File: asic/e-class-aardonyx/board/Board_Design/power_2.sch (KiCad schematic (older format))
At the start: 36 parts, among them Q1 FDN339AN, SW2 FSM2JSMAATR, U10 TPS7A7002DDAR, U11 ADM1085, U12 ADM1085, U13 TPS7A7002DDAR, U14 74AUP1G09GW

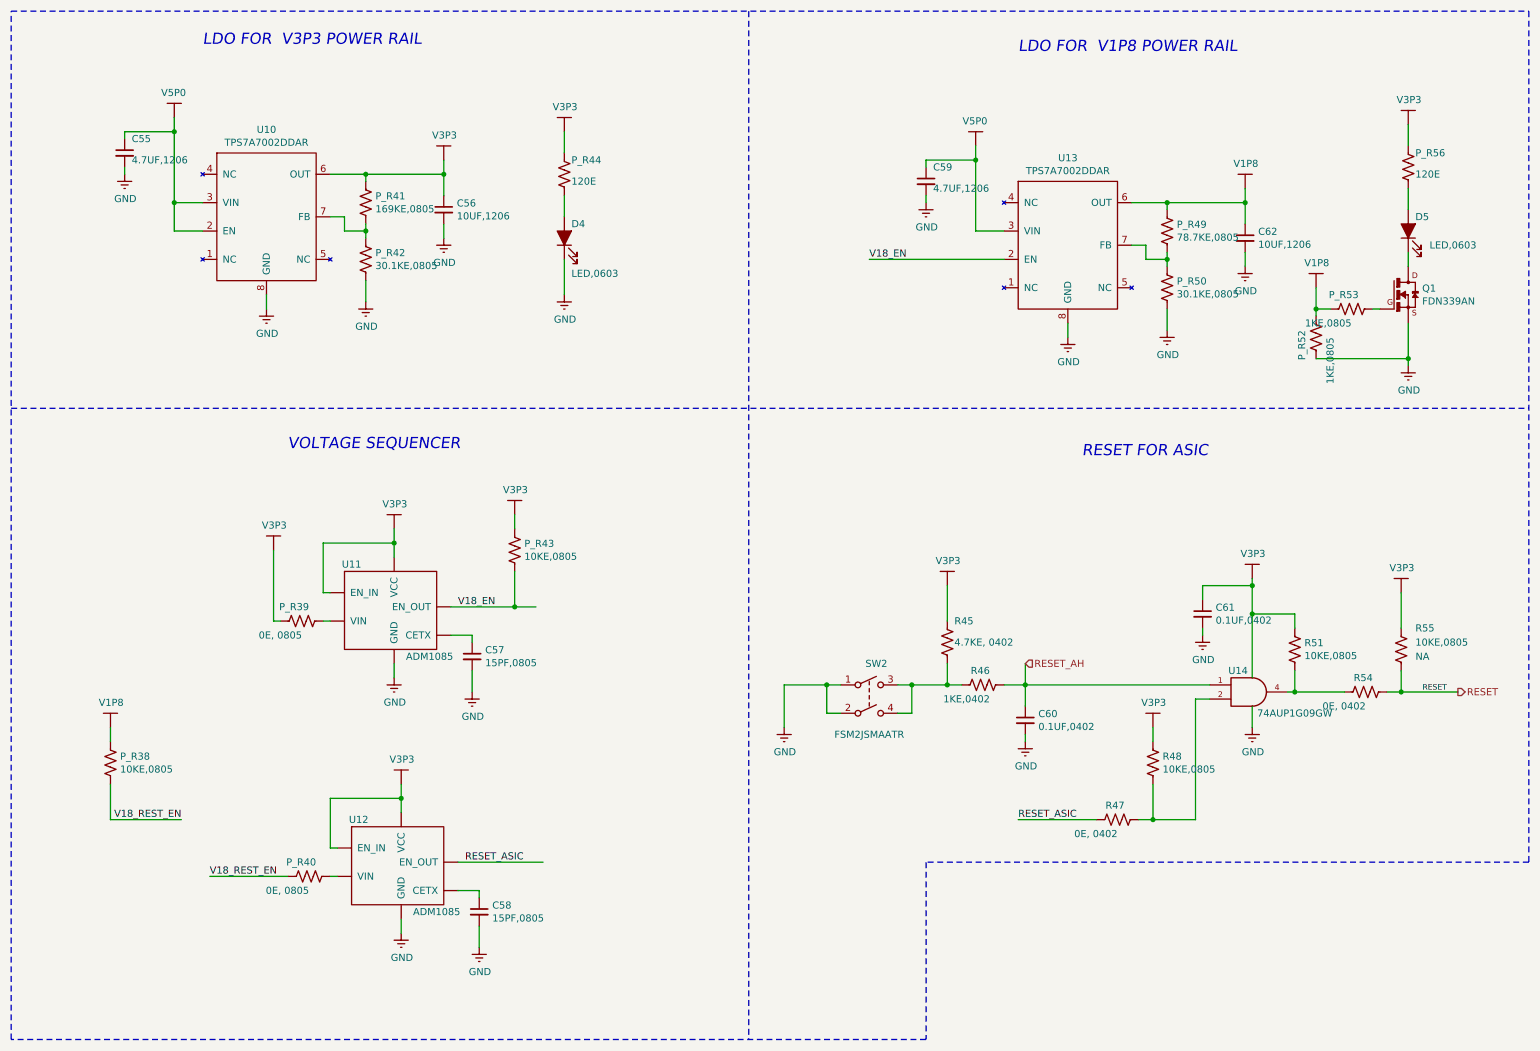
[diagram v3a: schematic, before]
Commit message: updated commented pending schematic
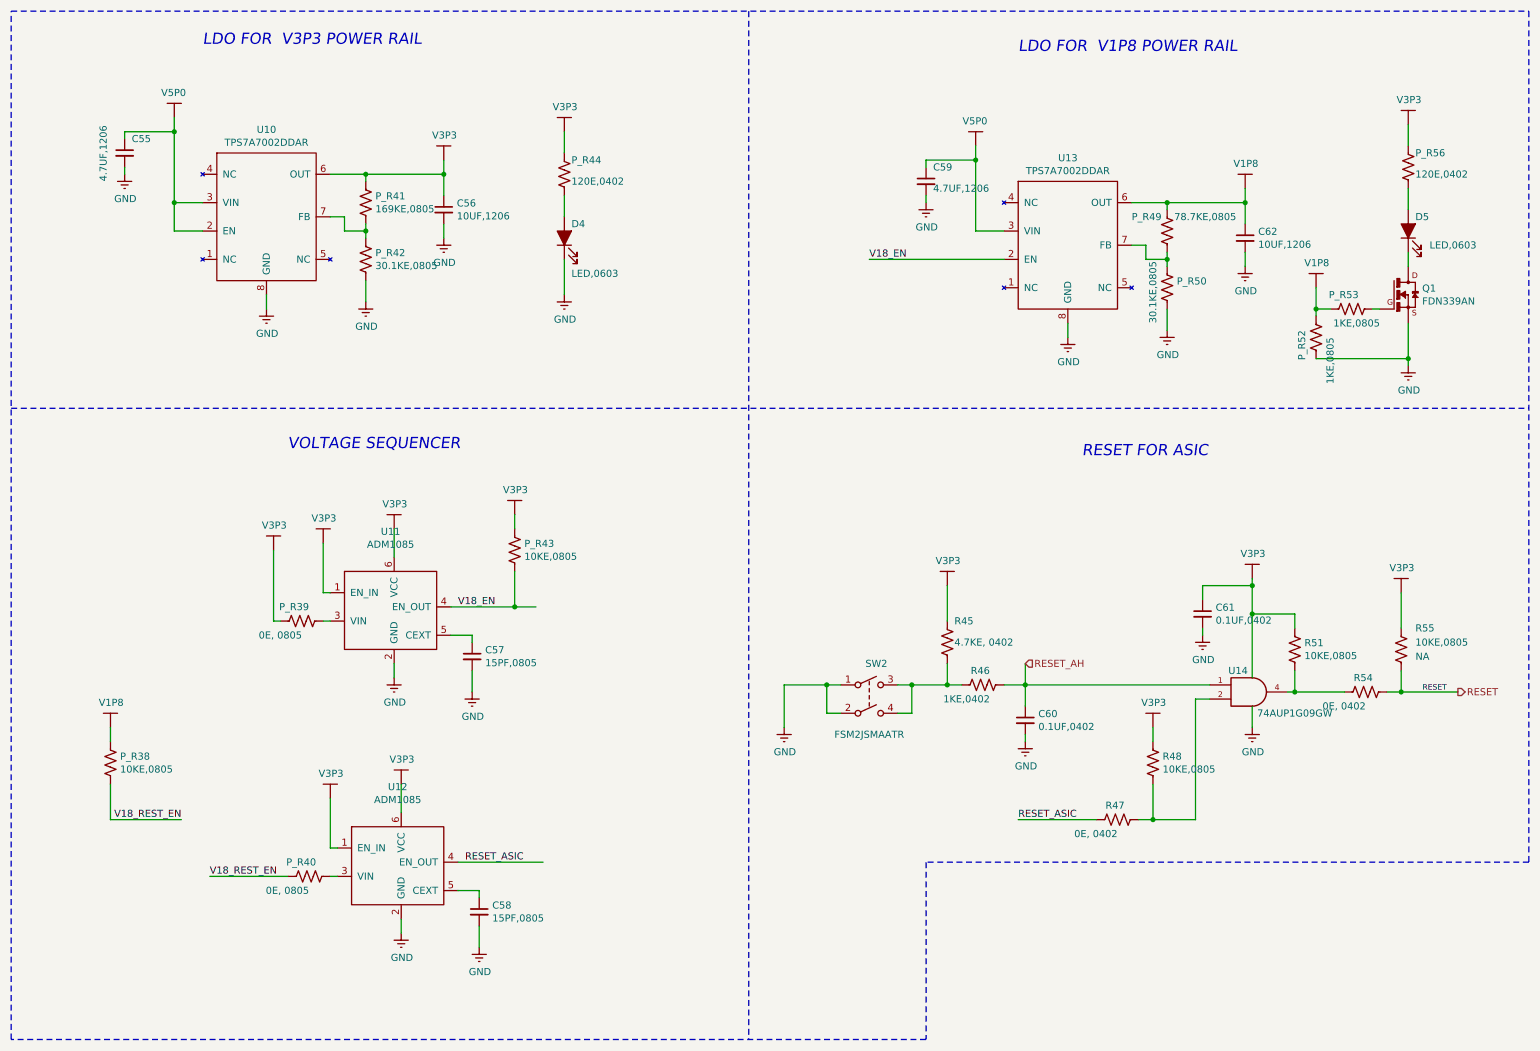
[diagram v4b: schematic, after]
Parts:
- removed U11, U12: ADM1085, symbol Aardonyx-rescue:ADM1085-aardonyx
- added U11, U12: ADM1085, symbol Aardonyx-rescue:ADM1085-skt32e_asic
- P_R44, P_R56: value 120E -> 120E,0402; Description RES SMD 120 OHM 5% 1/4W 1206 -> RES SMD 120 OHM 1% 1/16W 0402; Digikey PartNumber 311-120ERCT-ND -> 311-120LRCT-ND; Manufactured Part Number RC1206JR-07120RL -> RC0402FR-07120RL
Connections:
- net GND: now also U11.2 (GND), U12.2 (GND)
- net RESET_ASIC: now also U12.4 (EN_OUT)
- net V18_EN: now also U11.4 (EN_OUT)
- net at C57.1: now also U11.5 (CEXT)
- net at P_R39.2: now also U11.3 (VIN)
- net at C58.1: now also U12.5 (CEXT)
- net at P_R40.2: now also U12.3 (VIN)
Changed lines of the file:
@@
 AR Path="/5E6E93B2/5E722846" Ref="C55"  Part="1"
 F 0 "C55" H 1350 1600 50  0000 L CNN
-F 1 "4.7UF,1206" H 1350 1450 50  0000 L CNN
+F 1 "4.7UF,1206" V 1150 1300 50  0000 L CNN
 F 2 "" H 1300 1500 50  0001 C CNN
 F 3 "https://www.digikey.in/product-detail/en/kemet/T491A475K016AT/399-3697-1-ND/819022" H 1300 1500 50  0001 C CNN
@@
 AR Path="/5E6E93B2/5E7228B7" Ref="P_R44"  Part="1"
 F 0 "P_R44" H 4450 1750 50  0000 L CNN
-F 1 "120E" H 4450 1600 50  0000 L CNN
+F 1 "120E,0402" H 4450 1600 50  0000 L CNN
 F 2 "" V 4440 1640 50  0001 C CNN
 F 3 "https://www.digikey.in/product-detail/en/yageo/RC1206JR-07120RL/311-120ERCT-ND/732162" H 4400 1650 50  0001 C CNN
-F 4 "RES SMD 120 OHM 5% 1/4W 1206" H 4400 1650 50  0001 C CNN "Description"
-F 5 "311-120ERCT-ND" H 4400 1650 50  0001 C CNN "Digikey PartNumber"
-F 6 "RC1206JR-07120RL" H 4400 1650 50  0001 C CNN "Manufactured Part Number"
+F 4 "RES SMD 120 OHM 1% 1/16W 0402" H 4400 1650 50  0001 C CNN "Description"
+F 5 "311-120LRCT-ND" H 4400 1650 50  0001 C CNN "Digikey PartNumber"
+F 6 "RC0402FR-07120RL" H 4400 1650 50  0001 C CNN "Manufactured Part Number"
 F 7 "Yageo" H 4400 1650 50  0001 C CNN "Maufaturer"
 	1    4400 1650
@@
 	1    0    0    -1
 $EndComp
-$Comp
-L Aardonyx-rescue:ADM1085-aardonyx U11
-U 1 1 5E7753D3
-P 3200 4700
-F 0 "U11" H 2900 5000 50  0000 C CNN
-F 1 "ADM1085" H 3450 4350 50  0000 C CNN
-F 2 "" H 3100 4750 50  0001 C CNN
-F 3 "https://www.digikey.in/product-detail/en/analog-devices-inc/ADM1085AKSZ-REEL7/ADM1085AKSZ-REEL7CT-ND/820429" H 3100 4750 50  0001 C CNN
-F 4 "IC SUPERVISOR 1 CHANNEL SC70-6" H 3200 4700 50  0001 C CNN "Description"
-F 5 "ADM1085AKSZ-REEL7CT-ND" H 3200 4700 50  0001 C CNN "Digikey PartNumber"
-F 6 "ADM1085AKSZ-REEL7" H 3200 4700 50  0001 C CNN "Manufactured Part Number"
-F 7 "Analog Devices Inc." H 3200 4700 50  0001 C CNN "Maufaturer"
-	1    3200 4700
-	1    0    0    -1
-$EndComp
-Wire Wire Line
-	3200 4150 3200 4250
-Wire Wire Line
-	3200 4250 2700 4250
 Wire Wire Line
 	2700 4250 2700 4600
 Wire Wire Line
 	2700 4600 2750 4600
-Connection ~ 3200 4250
-Wire Wire Line
-	3200 4250 3200 4350
 Wire Wire Line
 	3750 5150 3750 5300
@@
 AR Path="/5DB8A7DC/5EC50B98" Ref="R?"  Part="1"
 AR Path="/5E6E93B2/5EC50B98" Ref="P_R49"  Part="1"
-F 0 "P_R49" H 8718 2096 50  0000 L CNN
-F 1 "78.7KE,0805" H 8718 2005 50  0000 L CNN
+F 0 "P_R49" H 8400 2150 50  0000 L CNN
+F 1 "78.7KE,0805" H 8700 2150 50  0000 L CNN
 F 2 "" V 8690 2040 50  0001 C CNN
 F 3 "https://www.digikey.in/product-detail/en/panasonic-electronic-components/ERA-6AEB7872V/P78-7KDACT-ND/3075252" H 8650 2050 50  0001 C CNN
@@
 AR Path="/5E6E93B2/5EC50B92" Ref="P_R50"  Part="1"
 F 0 "P_R50" H 8718 2496 50  0000 L CNN
-F 1 "30.1KE,0805" H 8718 2405 50  0000 L CNN
+F 1 "30.1KE,0805" V 8550 2200 50  0000 L CNN
 F 2 "" V 8690 2440 50  0001 C CNN
 F 3 "https://www.digikey.in/product-detail/en/panasonic-electronic-components/ERA-6AEB3012V/P30-1KDACT-ND/3075076" H 8650 2450 50  0001 C CNN
@@
 AR Path="/5E6E93B2/5EC66716" Ref="P_R56"  Part="1"
 F 0 "P_R56" H 10400 1700 50  0000 L CNN
-F 1 "120E" H 10400 1550 50  0000 L CNN
+F 1 "120E,0402" H 10400 1550 50  0000 L CNN
 F 2 "" V 10390 1590 50  0001 C CNN
 F 3 "https://www.digikey.in/product-detail/en/yageo/RC1206JR-07120RL/311-120ERCT-ND/732162" H 10350 1600 50  0001 C CNN
-F 4 "RES SMD 120 OHM 5% 1/4W 1206" H 10350 1600 50  0001 C CNN "Description"
-F 5 "311-120ERCT-ND" H 10350 1600 50  0001 C CNN "Digikey PartNumber"
-F 6 "RC1206JR-07120RL" H 10350 1600 50  0001 C CNN "Manufactured Part Number"
+F 4 "RES SMD 120 OHM 1% 1/16W 0402" H 10350 1600 50  0001 C CNN "Description"
+F 5 "311-120LRCT-ND" H 10350 1600 50  0001 C CNN "Digikey PartNumber"
+F 6 "RC0402FR-07120RL" H 10350 1600 50  0001 C CNN "Manufactured Part Number"
 F 7 "Yageo" H 10350 1600 50  0001 C CNN "Maufaturer"
 	1    10350 1600
@@
 AR Path="/5E6E93B2/5ECE41BC" Ref="P_R53"  Part="1"
 F 0 "P_R53" V 10050 2550 50  0000 L CNN
-F 1 "1KE,0805" V 9850 2600 50  0000 L CNN
+F 1 "1KE,0805" V 9850 2400 50  0000 L CNN
 F 2 "" V 9990 2590 50  0001 C CNN
 F 3 "https://www.digikey.in/product-detail/en/yageo/RC0805JR-071KL/311-1-0KARCT-ND/731165" H 9950 2600 50  0001 C CNN
@@
 	1    0    0    -1
 $EndComp
-$Comp
-L Aardonyx-rescue:ADM1085-aardonyx U12
-U 1 1 5ECF8040
-P 3250 6500
-F 0 "U12" H 2950 6800 50  0000 C CNN
-F 1 "ADM1085" H 3500 6150 50  0000 C CNN
-F 2 "" H 3150 6550 50  0001 C CNN
-F 3 "https://www.digikey.in/product-detail/en/analog-devices-inc/ADM1085AKSZ-REEL7/ADM1085AKSZ-REEL7CT-ND/820429" H 3150 6550 50  0001 C CNN
-F 4 "IC SUPERVISOR 1 CHANNEL SC70-6" H 3250 6500 50  0001 C CNN "Description"
-F 5 "ADM1085AKSZ-REEL7CT-ND" H 3250 6500 50  0001 C CNN "Digikey PartNumber"
-F 6 "ADM1085AKSZ-REEL7" H 3250 6500 50  0001 C CNN "Manufactured Part Number"
-F 7 "Analog Devices Inc." H 3250 6500 50  0001 C CNN "Maufaturer"
-	1    3250 6500
-	1    0    0    -1
-$EndComp
-Wire Wire Line
-	3250 5950 3250 6050
-Wire Wire Line
-	3250 6050 2750 6050
 Wire Wire Line
 	2750 6050 2750 6400
 Wire Wire Line
 	2750 6400 2800 6400
-Connection ~ 3250 6050
-Wire Wire Line
-	3250 6050 3250 6150
 Wire Wire Line
 	3800 6950 3800 7100
@@
 	1650 2050 1850 2050
 Connection ~ 1650 1850
+Wire Wire Line
+	3200 4150 3200 4350
+$Comp
+L Aardonyx-rescue:V3P3-skt32e_asic #PWR0141
+U 1 1 5EDD59E1
+P 2700 4250
+F 0 "#PWR0141" H 2850 4200 50  0001 C CNN
+F 1 "V3P3" H 2705 4425 50  0000 C CNN
+F 2 "" H 2700 4250 50  0001 C CNN
+F 3 "" H 2700 4250 50  0001 C CNN
+	1    2700 4250
+	1    0    0    -1
+$EndComp
+Wire Wire Line
+	3250 5950 3250 6150
+$Comp
+L Aardonyx-rescue:V3P3-skt32e_asic #PWR0142
+U 1 1 5EDD6599
+P 2750 6050
+F 0 "#PWR0142" H 2900 6000 50  0001 C CNN
+F 1 "V3P3" H 2755 6225 50  0000 C CNN
+F 2 "" H 2750 6050 50  0001 C CNN
+F 3 "" H 2750 6050 50  0001 C CNN
+	1    2750 6050
+	1    0    0    -1
+$EndComp
+$Comp
+L Aardonyx-rescue:ADM1085-skt32e_asic U11
+U 1 1 5EDDCF39
+P 3200 4700
+AR Path="/5EDDCF39" Ref="U11"  Part="1"
+AR Path="/5E6E93B2/5EDDCF39" Ref="U11"  Part="1"
+F 0 "U11" H 3175 5231 50  0000 C CNN
+F 1 "ADM1085" H 3175 5140 50  0000 C CNN
+F 2 "" H 3100 4750 50  0001 C CNN
+F 3 "" H 3100 4750 50  0001 C CNN
+	1    3200 4700
+	1    0    0    -1
+$EndComp
+$Comp
+L Aardonyx-rescue:ADM1085-skt32e_asic U12
+U 1 1 5EDDE10C
+P 3250 6500
+AR Path="/5EDDE10C" Ref="U12"  Part="1"
+AR Path="/5E6E93B2/5EDDE10C" Ref="U12"  Part="1"
+F 0 "U12" H 3225 7031 50  0000 C CNN
+F 1 "ADM1085" H 3225 6940 50  0000 C CNN
+F 2 "" H 3150 6550 50  0001 C CNN
+F 3 "" H 3150 6550 50  0001 C CNN
+	1    3250 6500
+	1    0    0    -1
+$EndComp
 $EndSCHEMATC

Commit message: updated footprint for netlist
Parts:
- C55, C56, C59, C62: footprint (none) -> Capacitor_SMD:C_1206_3216Metric
- C57, C58: footprint (none) -> Capacitor_SMD:C_0805_2012Metric
- C60, C61: footprint (none) -> Capacitor_SMD:C_0402_1005Metric
- D4, D5: footprint (none) -> LED_SMD:LED_0603_1608Metric
- P_R38, P_R39, P_R40, P_R41, P_R42, P_R43, P_R49, P_R50, P_R52, P_R53, R48, R51, R55: footprint (none) -> Resistor_SMD:R_0805_2012Metric
- P_R44, P_R56, R45, R46, R47, R54: footprint (none) -> Resistor_SMD:R_0402_1005Metric
- U10, U13: footprint (none) -> Package_SO:SOIC-8-1EP_3.9x4.9mm_P1.27mm_EP2.29x3mm_ThermalVias

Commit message: Updated schematic
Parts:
- removed P_R52, P_R53: 1KE,0805, Resistor_SMD:R_0805_2012Metric, symbol Aardonyx-rescue:R_US-aardonyx
- added P_R1, P_R2: 0.02E,2512, Resistor_SMD:R_0402_1005Metric, symbol Aardonyx-rescue:R_US-aardonyx
- added R40, R41: 1KE,0402, Resistor_SMD:R_0805_2012Metric, symbol Aardonyx-rescue:R_US-aardonyx
- C55, C59: Description CAP TANT 4.7UF 10% 16V 1206 -> CAP TANT 4.7UF 10% 16V 1206; Digikey PartNumber 399-3697-1-ND -> 399-3697-1-ND; Manufactured Part Number T491A475K016AT -> T491A475K016AT
- D4, D5: value LED,0603 -> LED,1206; Description LED GREEN CLEAR CHIP SMD -> LED GREEN DIFFUSED 1206 SMD; Digikey PartNumber 160-1832-1-ND -> 67-1002-1-ND; Manufactured Part Number LTST-C193TGKT-5A -> SML-LX1206GW-TR; Maufaturer Lite-On Inc. -> Lumex Opto/Components Inc.
- P_R44: value 120E,0402 -> 220E,0402
- U11, U12: Description (none) -> IC SUPERVISOR 1 CHANNEL SC70-6; Digikey PartNumber (none) -> ADM1085AKSZ-REEL7CT-ND; Manufactured Part Number (none) -> ADM1085AKSZ-REEL7; Maufaturer (none) -> Analog Devices Inc.
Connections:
- net GND: now also R40.2
- net at P_R41.1, U10.6 (OUT): now also P_R1.2; no longer C56.1
- net at P_R49.1, U13.6 (OUT): now also P_R2.2; no longer C62.1
- net at Q1.1 (G): now also R41.1
- new net: C56.1, P_R1.1
- new net: C62.1, P_R2.1
- new net: R40.1, R41.2
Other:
- note added: "5V TO 1.8V LDO"
- note added: "5V TO 3.3V LDO"
- note added: "SKT32E HARDWARE RESET"
- note added: "SKT32E PMIC (VOLTAGE SEQUENCER)"
- note removed: "LDO FOR V1P8 POWER RAIL"
- note removed: "LDO FOR V3P3 POWER RAIL"
- note removed: "RESET FOR ASIC"
- note removed: "VOLTAGE SEQUENCER"
- moved on the sheet: C56, C59, C62, D4, D5, P_R44, P_R49, P_R50, P_R56, U13

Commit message: Update Footprint
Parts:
- Q1: footprint SSOT-3 -> Package_TO_SOT_SMD:SuperSOT-3
- SW2: footprint (none) -> Aardonyx:SW_PUSH_SPST_NO_4.5MM_7MM
- U11, U12: footprint (none) -> Package_SO:SC-74-6_1.5x2.9mm_P0.95mm
- U14: footprint (none) -> Package_TO_SOT_SMD:SOT-353_SC-70-5_Handsoldering
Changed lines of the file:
@@
 EESchema Schematic File Version 4
-LIBS:Aardonyx-cache
-EELAYER 29 0
+EELAYER 30 0
 EELAYER END
 $Descr A4 11693 8268
@@
 F 0 "U14" H 9150 5450 50  0000 C CNN
 F 1 "74AUP1G09GW" H 9550 5150 50  0000 C CNN
-F 2 "" H 9250 5300 50  0001 C CNN
+F 2 "Package_TO_SOT_SMD:SOT-353_SC-70-5_Handsoldering" H 9250 5300 50  0001 C CNN
 F 3 "https://www.digikey.in/product-detail/en/nexperia-usa-inc/74AUP1G09GW-125/1727-4492-1-ND/2530869" H 9250 5300 50  0001 C CNN
 F 4 "IC GATE AND 1CH 2-INP 5TSSOP" H 9250 5300 50  0001 C CNN "Description"
@@
 F 0 "SW2" H 6600 5600 50  0000 C CNN
 F 1 "FSM2JSMAATR " H 6550 5100 50  0000 C CNN
-F 2 "" H 6550 5350 50  0001 C CNN
+F 2 "Aardonyx:SW_PUSH_SPST_NO_4.5MM_7MM" H 6550 5350 50  0001 C CNN
 F 3 "https://www.digikey.com/product-detail/en/te-connectivity-alcoswitch-switches/FSM2JSMAATR/450-1792-1-ND/3503931" H 6550 5350 50  0001 C CNN
 F 4 "SWITCH TACTILE SPST-NO 0.05A 24V" H 6550 5350 50  0001 C CNN "Description"
@@
 F 0 "U11" H 3175 5231 50  0000 C CNN
 F 1 "ADM1085" H 3175 5140 50  0000 C CNN
-F 2 "" H 3100 4750 50  0001 C CNN
+F 2 "Package_SO:SC-74-6_1.5x2.9mm_P0.95mm" H 3100 4750 50  0001 C CNN
 F 3 "https://www.mouser.in/ProductDetail/Analog-Devices/ADM1085AKSZ-REEL7?qs=sGAEpiMZZMv9Q1JI0Mo%2FtdiYL5rCVCWC (or)  https://www.digikey.com/product-detail/en/analog-devices-inc/ADM1085AKSZ-REEL7/ADM1085AKSZ-REEL7CT-ND/820429" H 3100 4750 50  0001 C CNN
 F 4 "IC SUPERVISOR 1 CHANNEL SC70-6" H 3200 4700 50  0001 C CNN "Description"
@@
 F 0 "U12" H 3225 7031 50  0000 C CNN
 F 1 "ADM1085" H 3225 6940 50  0000 C CNN
-F 2 "" H 3150 6550 50  0001 C CNN
+F 2 "Package_SO:SC-74-6_1.5x2.9mm_P0.95mm" H 3150 6550 50  0001 C CNN
 F 3 "https://www.mouser.in/ProductDetail/Analog-Devices/ADM1085AKSZ-REEL7?qs=sGAEpiMZZMv9Q1JI0Mo%2FtdiYL5rCVCWC (or)  https://www.digikey.com/product-detail/en/analog-devices-inc/ADM1085AKSZ-REEL7/ADM1085AKSZ-REEL7CT-ND/820429" H 3150 6550 50  0001 C CNN
 F 4 "IC SUPERVISOR 1 CHANNEL SC70-6" H 3250 6500 50  0001 C CNN "Description"
@@
 F 0 "Q1" H 10598 2396 50  0000 L CNN
 F 1 "FDN339AN" H 10598 2305 50  0000 L CNN
-F 2 "SSOT-3" H 10500 2350 50  0001 L BNN
+F 2 "Package_TO_SOT_SMD:SuperSOT-3" H 10500 2350 50  0001 L BNN
 F 3 "https://www.digikey.com/product-detail/en/on-semiconductor/FDN339AN/FDN339ANCT-ND/965603" H 10500 2350 50  0001 C CNN
 F 4 "MOSFET N-CH 20V 3A SSOT3" H 10500 2350 50  0001 C CNN "Description"

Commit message: Updated footprint association
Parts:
- P_R1, P_R2: footprint Resistor_SMD:R_0402_1005Metric -> Resistor_SMD:R_2512_6332Metric
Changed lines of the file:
@@
 EESchema Schematic File Version 4
-EELAYER 30 0
+LIBS:Aardonyx-cache
+EELAYER 29 0
 EELAYER END
 $Descr A4 11693 8268
@@
 F 0 "P_R2" V 8600 1500 50  0000 L CNN
 F 1 "0.02E,2512" V 8700 2000 50  0000 L CNN
-F 2 "Resistor_SMD:R_0402_1005Metric" V 8690 1840 50  0001 C CNN
+F 2 "Resistor_SMD:R_2512_6332Metric" V 8690 1840 50  0001 C CNN
 F 3 "https://www.digikey.com/product-detail/en/yageo/PA2512FKF7W0R002E/YAG2142CT-ND/5139590" H 8650 1850 50  0001 C CNN
 F 4 "RES 0.002 OHM 1% 2W 2512" H 8650 1850 50  0001 C CNN "Description"
@@
 F 0 "P_R1" V 3550 1300 50  0000 L CNN
 F 1 "0.02E,2512" V 3650 1800 50  0000 L CNN
-F 2 "Resistor_SMD:R_0402_1005Metric" V 3640 1640 50  0001 C CNN
+F 2 "Resistor_SMD:R_2512_6332Metric" V 3640 1640 50  0001 C CNN
 F 3 "https://www.digikey.com/product-detail/en/yageo/PA2512FKF7W0R002E/YAG2142CT-ND/5139590" H 3600 1650 50  0001 C CNN
 F 4 "RES 0.002 OHM 1% 2W 2512" H 3600 1650 50  0001 C CNN "Description"
